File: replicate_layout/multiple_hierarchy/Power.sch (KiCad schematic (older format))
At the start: 8 parts, among them Q301 CSD19531KCS, Q302 CSD19531KCS, U301 IR2181

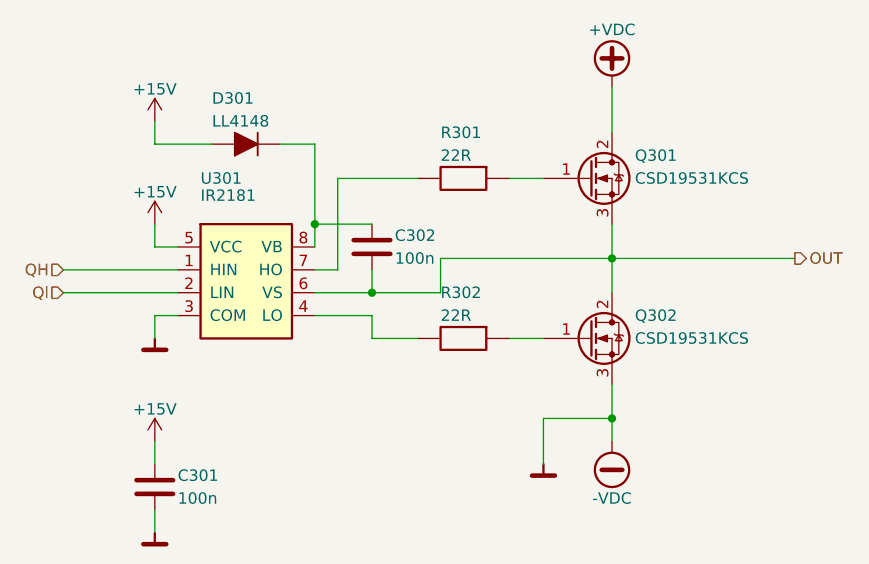
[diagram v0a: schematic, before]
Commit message: Changed test project to include complex hierarchy
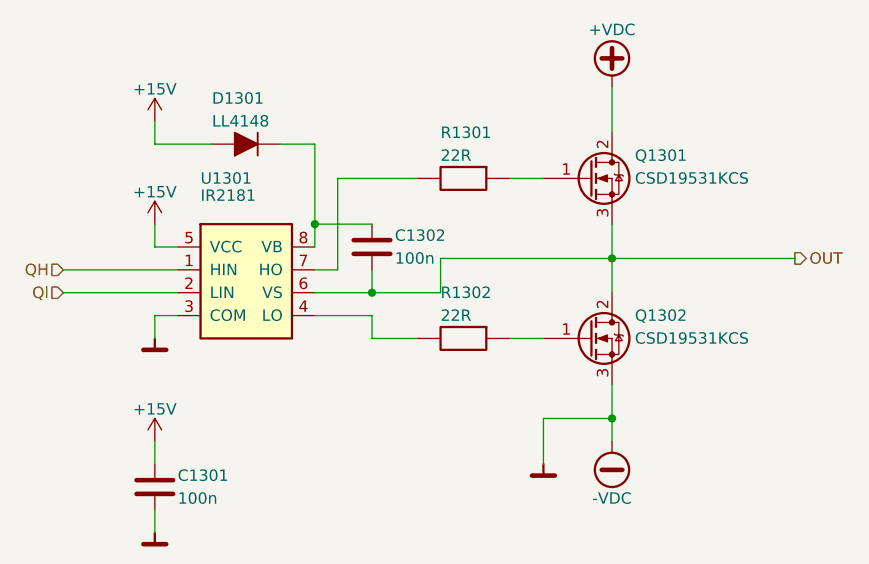
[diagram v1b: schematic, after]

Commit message: Working V2 revision
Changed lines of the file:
@@
 EESchema Schematic File Version 4
 LIBS:multiple_hierarchy-cache
-EELAYER 26 0
+EELAYER 29 0
 EELAYER END
 $Descr A4 11693 8268
 encoding utf-8
-Sheet 11 13
+Sheet 14 14
 Title ""
 Date ""
@@
 AR Path="/5B76D023/5B772791/5B768070" Ref="Q901"  Part="1"
 AR Path="/5B76D031/5B772791/5B768070" Ref="Q1301"  Part="1"
-F 0 "Q1301" H 3700 2550 50  0000 L CNN
+AR Path="/5C575278/5B768070" Ref="Q1401"  Part="1"
+F 0 "Q1401" H 3700 2550 50  0000 L CNN
 F 1 "CSD19531KCS" H 3700 2450 50  0000 L CNN
 F 2 "Discretes:TO-220" H 3700 2350 50  0001 L CNN
@@
 AR Path="/5B76D023/5B772791/5B768110" Ref="Q902"  Part="1"
 AR Path="/5B76D031/5B772791/5B768110" Ref="Q1302"  Part="1"
-F 0 "Q1302" H 3700 3250 50  0000 L CNN
+AR Path="/5C575278/5B768110" Ref="Q1402"  Part="1"
+F 0 "Q1402" H 3700 3250 50  0000 L CNN
 F 1 "CSD19531KCS" H 3700 3150 50  0000 L CNN
 F 2 "Discretes:TO-220" H 3700 3050 50  0001 L CNN
@@
 AR Path="/5B76D023/5B772791/5B768171" Ref="U901"  Part="1"
 AR Path="/5B76D031/5B772791/5B768171" Ref="U1301"  Part="1"
-F 0 "U1301" H 1800 3250 50  0000 L CNN
+AR Path="/5C575278/5B768171" Ref="U1401"  Part="1"
+F 0 "U1401" H 1800 3250 50  0000 L CNN
 F 1 "IR2181" H 1800 3175 50  0000 L CNN
 F 2 "Package_SO:SO8" H 1800 3100 50  0001 L CNN
@@
 AR Path="/5B76D023/5B772791/5B768234" Ref="R901"  Part="1"
 AR Path="/5B76D031/5B772791/5B768234" Ref="R1301"  Part="1"
-F 0 "R1301" H 2850 2650 50  0000 L CNN
+AR Path="/5C575278/5B768234" Ref="R1401"  Part="1"
+F 0 "R1401" H 2850 2650 50  0000 L CNN
 F 1 "22R" H 2850 2550 50  0000 L CNN
 F 2 "Passives:R1206M" H 2850 2350 50  0001 L CNN
@@
 AR Path="/5B76D023/5B772791/5B7682C5" Ref="R902"  Part="1"
 AR Path="/5B76D031/5B772791/5B7682C5" Ref="R1302"  Part="1"
-F 0 "R1302" H 2850 3350 50  0000 L CNN
+AR Path="/5C575278/5B7682C5" Ref="R1402"  Part="1"
+F 0 "R1402" H 2850 3350 50  0000 L CNN
 F 1 "22R" H 2850 3250 50  0000 L CNN
 F 2 "Passives:R1206M" H 2850 3050 50  0001 L CNN
@@
 AR Path="/5B76D023/5B772791/5B768355" Ref="#PWR0907"  Part="1"
 AR Path="/5B76D031/5B772791/5B768355" Ref="#PWR01307"  Part="1"
-F 0 "#PWR01307" H 3600 1950 50  0001 C CNN
+AR Path="/5C575278/5B768355" Ref="#PWR01407"  Part="1"
+F 0 "#PWR01407" H 3600 1950 50  0001 C CNN
 F 1 "+VDC" H 3600 2300 50  0000 C CNN
 F 2 "" H 3600 2050 50  0001 C CNN
@@
 AR Path="/5B76D023/5B772791/5B768396" Ref="#PWR0908"  Part="1"
 AR Path="/5B76D031/5B772791/5B768396" Ref="#PWR01308"  Part="1"
-F 0 "#PWR01308" H 3600 3500 50  0001 C CNN
+AR Path="/5C575278/5B768396" Ref="#PWR01408"  Part="1"
+F 0 "#PWR01408" H 3600 3500 50  0001 C CNN
 F 1 "-VDC" H 3600 3850 50  0000 C CNN
 F 2 "" H 3600 3600 50  0001 C CNN
@@
 AR Path="/5B76D023/5B772791/5B7685DA" Ref="C901"  Part="1"
 AR Path="/5B76D031/5B772791/5B7685DA" Ref="C1301"  Part="1"
-F 0 "C1301" H 1700 3850 50  0000 L CNN
+AR Path="/5C575278/5B7685DA" Ref="C1401"  Part="1"
+F 0 "C1401" H 1700 3850 50  0000 L CNN
 F 1 "100n" H 1700 3750 50  0000 L CNN
 F 2 "Passives:C1206M" H 1650 3700 50  0001 L CNN
@@
 AR Path="/5B76D023/5B772791/5B7686C7" Ref="C902"  Part="1"
 AR Path="/5B76D031/5B772791/5B7686C7" Ref="C1302"  Part="1"
-F 0 "C1302" H 2650 2800 50  0000 L CNN
+AR Path="/5C575278/5B7686C7" Ref="C1402"  Part="1"
+F 0 "C1402" H 2650 2800 50  0000 L CNN
 F 1 "100n" H 2650 2700 50  0000 L CNN
 F 2 "Passives:C1206M" H 2600 2650 50  0001 L CNN
@@
 AR Path="/5B76D023/5B772791/5B7687F1" Ref="#PWR0902"  Part="1"
 AR Path="/5B76D031/5B772791/5B7687F1" Ref="#PWR01302"  Part="1"
-F 0 "#PWR01302" H 1600 2500 50  0001 C CNN
+AR Path="/5C575278/5B7687F1" Ref="#PWR01402"  Part="1"
+F 0 "#PWR01402" H 1600 2500 50  0001 C CNN
 F 1 "+15V" H 1600 2790 50  0000 C CNN
 F 2 "" H 1600 2650 50  0001 C CNN
@@
 AR Path="/5B76D023/5B772791/5B76894E" Ref="#PWR0904"  Part="1"
 AR Path="/5B76D031/5B772791/5B76894E" Ref="#PWR01304"  Part="1"
-F 0 "#PWR01304" H 1600 3450 50  0001 C CNN
+AR Path="/5C575278/5B76894E" Ref="#PWR01404"  Part="1"
+F 0 "#PWR01404" H 1600 3450 50  0001 C CNN
 F 1 "+15V" H 1600 3740 50  0000 C CNN
 F 2 "" H 1600 3600 50  0001 C CNN
@@
 AR Path="/5B76D023/5B772791/5B768A80" Ref="#PWR0903"  Part="1"
 AR Path="/5B76D031/5B772791/5B768A80" Ref="#PWR01303"  Part="1"
-F 0 "#PWR01303" H 1600 3000 50  0001 C CNN
+AR Path="/5C575278/5B768A80" Ref="#PWR01403"  Part="1"
+F 0 "#PWR01403" H 1600 3000 50  0001 C CNN
 F 1 "GND" H 1750 3100 50  0001 C CNN
 F 2 "" H 1600 3150 50  0001 C CNN
@@
 AR Path="/5B76D023/5B772791/5B768BE1" Ref="#PWR0905"  Part="1"
 AR Path="/5B76D031/5B772791/5B768BE1" Ref="#PWR01305"  Part="1"
-F 0 "#PWR01305" H 1600 3850 50  0001 C CNN
+AR Path="/5C575278/5B768BE1" Ref="#PWR01405"  Part="1"
+F 0 "#PWR01405" H 1600 3850 50  0001 C CNN
 F 1 "GND" H 1750 3950 50  0001 C CNN
 F 2 "" H 1600 4000 50  0001 C CNN
@@
 AR Path="/5B76D023/5B772791/5B769358" Ref="#PWR0901"  Part="1"
 AR Path="/5B76D031/5B772791/5B769358" Ref="#PWR01301"  Part="1"
-F 0 "#PWR01301" H 1600 2050 50  0001 C CNN
+AR Path="/5C575278/5B769358" Ref="#PWR01401"  Part="1"
+F 0 "#PWR01401" H 1600 2050 50  0001 C CNN
 F 1 "+15V" H 1600 2340 50  0000 C CNN
 F 2 "" H 1600 2200 50  0001 C CNN
@@
 AR Path="/5B76D023/5B772791/5B76A6F5" Ref="D901"  Part="1"
 AR Path="/5B76D031/5B772791/5B76A6F5" Ref="D1301"  Part="1"
-F 0 "D1301" H 2150 2100 50  0000 R CNN
+AR Path="/5C575278/5B76A6F5" Ref="D1401"  Part="1"
+F 0 "D1401" H 2150 2100 50  0000 R CNN
 F 1 "LL4148" H 2150 2200 50  0000 R CNN
 F 2 "Discretes:D_MiniMELF" H 1900 2200 50  0001 L CNN
@@
 AR Path="/5B76D023/5B772791/5B7764D3" Ref="#PWR0906"  Part="1"
 AR Path="/5B76D031/5B772791/5B7764D3" Ref="#PWR01306"  Part="1"
-F 0 "#PWR01306" H 3300 3550 50  0001 C CNN
+AR Path="/5C575278/5B7764D3" Ref="#PWR01406"  Part="1"
+F 0 "#PWR01406" H 3300 3550 50  0001 C CNN
 F 1 "GND" H 3450 3650 50  0001 C CNN
 F 2 "" H 3300 3700 50  0001 C CNN
